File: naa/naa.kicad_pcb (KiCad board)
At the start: 2 copper layers, 20 parts, among them X1 Контрольная_точка_сопряжения, X2 Контрольная_точка_сопряжения

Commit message: готова схема, добавлены gerber и pdf
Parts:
- added C4: Конденсатор_16В_0.1_мкФ+-10проц., MOTOR_RLC:Конденсатор_SMD_К10-83(0603), F.Cu at (130.8, 71.2)
- added C5: Конденсатор_подстроечный_TZC3R100A110, N_RLC:Конденсатор_подстроечный_TZC3, F.Cu at (180.2, 69.8)
- added C6: Конденсатор_подстроечный_TZC3R100A110, N_RLC:Конденсатор_подстроечный_TZC3, F.Cu at (189.8, 71.2)
- added D1: LOGO, N_ICO:el-nikitos_19x7, F.Cu at (162.0, 66.2)
- added L4: Чип-индуктивность_2,2_мкГн±10%, N_RLC:Чип-индуктивность_SMD_0805, F.Cu at (180.5, 76.0)
- added L5: Чип-индуктивность_2,2_мкГн±10%, N_RLC:Чип-индуктивность_SMD_0805, F.Cu at (189.8, 66.0)
- added R7: Резистор_10_кОм±5%_0,1Вт, MOTOR_RLC:Резистор_SMD_0603-0,075_Вт, F.Cu at (172.8, 66.2)
- added R8: Резистор_10_кОм±5%_0,1Вт, MOTOR_RLC:Резистор_SMD_0603-0,075_Вт, F.Cu at (175.2, 74.0)
- added R9: Резистор_470_Ом±5%_0,1Вт, MOTOR_RLC:Резистор_SMD_0603-0,075_Вт, F.Cu at (196.0, 74.2)
- added RP2: Резистор_подстроечный_PVA3A102, MOTOR_IMPORT_OTK:резистор_подстроечный_PVZ3A334, F.Cu at (147.6, 74.8)
- added RP3: Резистор_подстроечный_PVZ3A105, MOTOR_IMPORT_OTK:резистор_подстроечный_PVZ3A334, F.Cu at (171.0, 75.2)
- added RP4: Резистор_подстроечный_PVA3A102, MOTOR_IMPORT_OTK:резистор_подстроечный_PVZ3A334, F.Cu at (185.6, 75.0)
- added VT2: Транзистор_КТ368Б9, MOTOR_VD_VT_HL:Корпус_КТ-46, F.Cu at (176.8, 68.8)
- added X3: Контрольная_точка_сопряжения, MOTOR_X:Пробник, F.Cu at (182.8, 74.8)
- added X4: Контрольная_точка_сопряжения, MOTOR_X:Пробник, F.Cu at (196.0, 71.0)
- added XP5: Вилка_PLS-2, N_X:Вилка_PLS2_вертикальная, F.Cu at (181.2, 65.8)
- added XP6: Вилка_PLS-2, N_X:Вилка_PLS2_вертикальная, F.Cu at (177.8, 73.2)
- added XP7: Вилка_PLS-3, N_X:Вилка_PLS3_вертикальная, F.Cu at (193.2, 69.0)
- added XS1: Розетка_KLS1-SMA001, N_X:Розетка_KLS1-SMA001, F.Cu at (119.4, 71.8)
- added XS2: Розетка_KLS1-SMA001, N_X:Розетка_KLS1-SMA001, F.Cu at (160.7, 71.2)
- added XS3: Розетка_KLS1-SMA001, N_X:Розетка_KLS1-SMA001, F.Cu at (198.7, 70.2)
- R5: value Резистор_470_Ом±5%_0,1Вт -> Резистор_1_кОм±5%_0,1Вт
- moved R1 58.7 mm to (128.0, 75.0), turned to 270 degrees
- moved L1 55.6 mm to (122.2, 66.5)
- moved C1 53.3 mm to (128.0, 67.8), turned to 270 degrees
- moved XP1 48.7 mm to (116.2, 65.8), turned to 270 degrees
- moved L3 41.1 mm to (148.5, 65.8)
- moved XP4 38.7 mm to (155.2, 71.5), turned to 270 degrees
- moved C3 37.2 mm to (151.8, 71.2), turned to 270 degrees
- moved R6 27.5 mm to (158.0, 74.2), turned to 270 degrees
- moved XP2 26.8 mm to (143.2, 65.8)
- moved R5 26.1 mm to (172.5, 71.8), turned to 90 degrees
- moved X2 24.7 mm to (158.0, 71.0), turned to 90 degrees
- moved RP1 5.35 mm to (133.0, 75.2)
- moved R3 1.60 mm to (134.8, 66.2)
- moved R2 1.06 mm to (134.5, 71.8), turned to 90 degrees
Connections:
- R3 pad 1: /kaskad_1/5V -> /5V
- R4 pad 2: /kaskad_1/GND -> /GND
- R5 pad 1: Net-(C2-Pad2) -> /kaskad_2/INPUT
- R5 pad 2: /kaskad_1/GND -> Net-(R5-Pad2)
- R6 pad 2: /kaskad_1/GND -> /GND
- RP1 pad 1: /kaskad_1/5V -> /5V
- RP1 pad 3: /kaskad_1/GND -> /GND
- XP1 pad 2: Net-(L1-Pad1) -> Net-(XP1-Pad2)
- XP4 pad 1: /kaskad_1/OUTPUT -> /kaskad_2/INPUT
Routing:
- net /kaskad_2/INPUT: track 0.00 -> 30.7 mm, vias 0 -> 1
- net /GND: track 0.00 -> 24.9 mm, vias 0 -> 8
- net /5V: track 0.00 -> 17.9 mm
- net Net-(C1-Pad2): track 0.00 -> 15.5 mm
- net /kaskad_2/OUTPUT: track 0.00 -> 13.2 mm
- net Net-(C5-Pad2): track 0.00 -> 12.4 mm
- net Net-(C6-Pad2): track 0.00 -> 9.54 mm
- net Net-(R6-Pad1): track 0.00 -> 8.20 mm
- net /kaskad_2/AMP_1: track 0.00 -> 8.16 mm
- net /kaskad_1/AMP_1: track 0.00 -> 8.16 mm
- net Net-(L5-Pad1): track 0.00 -> 7.48 mm
- net Net-(C3-Pad2): track 0.00 -> 7.04 mm
- net Net-(L1-Pad1): track 0.00 -> 6.74 mm
- net Net-(C3-Pad1): track 0.00 -> 6.46 mm
- net Net-(R8-Pad1): track 0.00 -> 6.35 mm
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- added copper zone on F.Cu, net (none)
- added copper zone on F.Cu, net /5V
- added copper zone on B.Cu, net /GND
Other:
- board outline added: 93 x 16 mm
- board text added: "40,660 ... 40,7 МГц: 40,680 МГц"
- board text added: "NAA.0.M5"
- board text removed: "40,660 ... 40,7 МГц 40,680 МГц"

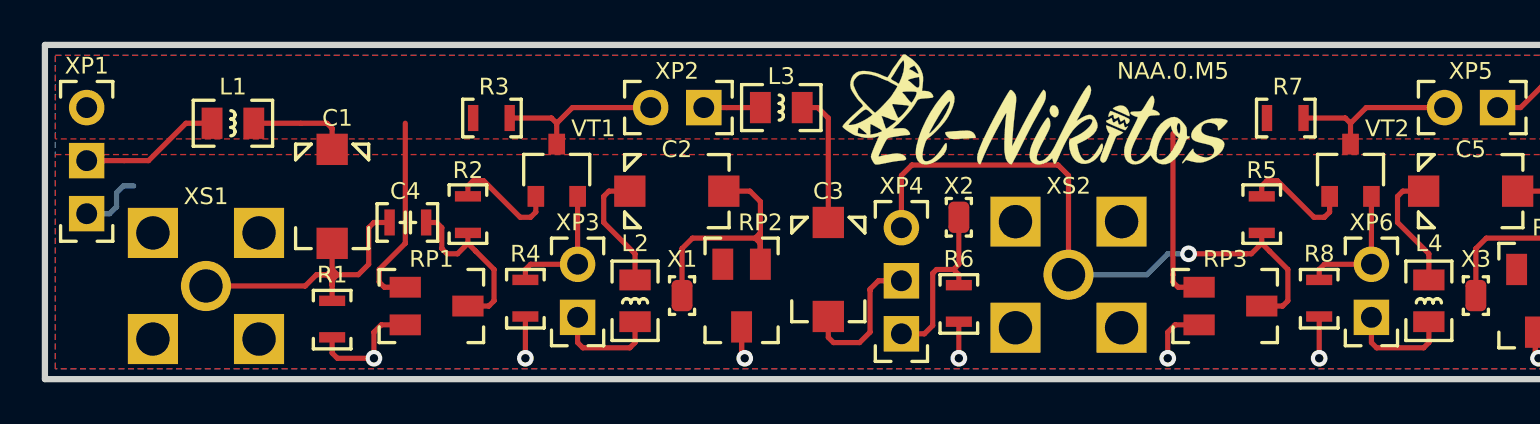
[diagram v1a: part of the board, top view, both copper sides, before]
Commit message: добавлены кондеи на питание, обновлены gerber и pdf
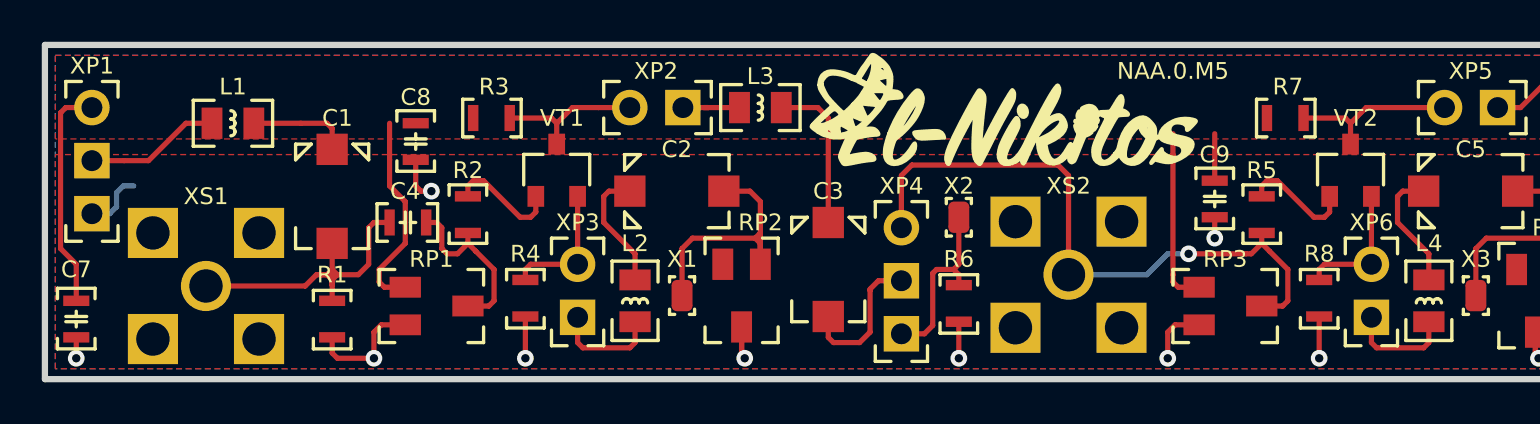
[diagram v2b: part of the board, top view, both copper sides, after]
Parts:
- added C7: Конденсатор_16В_0.1_мкФ+-10проц., MOTOR_RLC:Конденсатор_SMD_К10-83(0603), F.Cu at (115.8, 75.0)
- added C8: Конденсатор_16В_0.1_мкФ+-10проц., MOTOR_RLC:Конденсатор_SMD_К10-83(0603), F.Cu at (132.0, 66.5)
- added C9: Конденсатор_16В_0.1_мкФ+-10проц., MOTOR_RLC:Конденсатор_SMD_К10-83(0603), F.Cu at (170.2, 69.2)
- moved D1 1.50 mm to (160.5, 66.2)
- moved L3 1.00 mm to (147.5, 65.8)
- moved XP2 1.00 mm to (142.2, 65.8)
- moved XP1 0.25 mm to (116.5, 65.8)
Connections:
- XP1 pad 2: Net-(XP1-Pad2) -> Net-(L1-Pad1)
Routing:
- net /5V: track 17.9 -> 31.1 mm
- net /GND: track 24.9 -> 29.0 mm, vias 8 -> 11
- net Net-(C3-Pad1): track 6.46 -> 7.46 mm
- net /kaskad_1/AMP_1: track 8.16 -> 7.16 mm
